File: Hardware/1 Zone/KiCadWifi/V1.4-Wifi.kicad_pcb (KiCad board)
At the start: 2 copper layers, 100 x 80 mm, 134 parts, among them CN11 Pinheader 1x02 P2.54 Horizont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, CN16 Pinheader 1x02 P2.54 Horizont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, Q1 AOD4184A, Q10 PJA3404A, Q11 PJA3404A, Q12 BC816-16VL, Q8 UMH3NTN, SW1 K2-1102DP-G3SW-04, SW2 K2-1102DP-G3SW-04, SW3 K2-1102DP-G3SW-04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

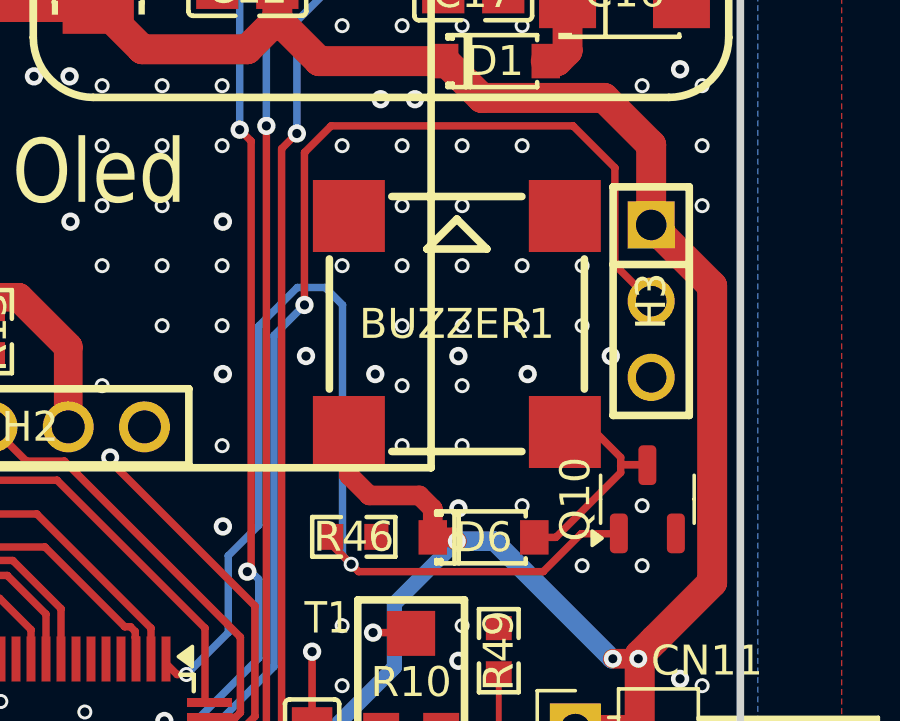
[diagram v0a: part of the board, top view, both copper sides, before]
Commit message: Replace Buzzer1 with CMT-8504-100-SMT-TR
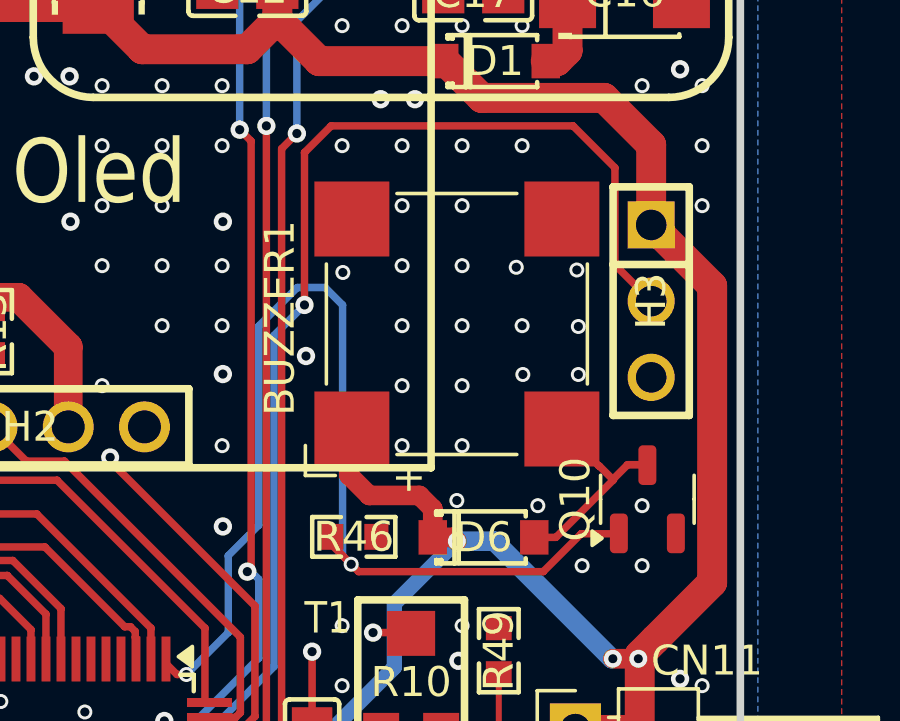
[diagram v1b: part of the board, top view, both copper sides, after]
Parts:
- BUZZER1: footprint V1.4-Wifi-easyedapro:BUZ-SMD_4P-L8.5-W8.5-P8.50-BR -> Buzzer_Beeper:MagneticBuzzer_CUI_CMT-8504-100-SMT
- turned BUZZER1 to 90 degrees
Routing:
- net THERMISTOR3: vias 2 -> 0

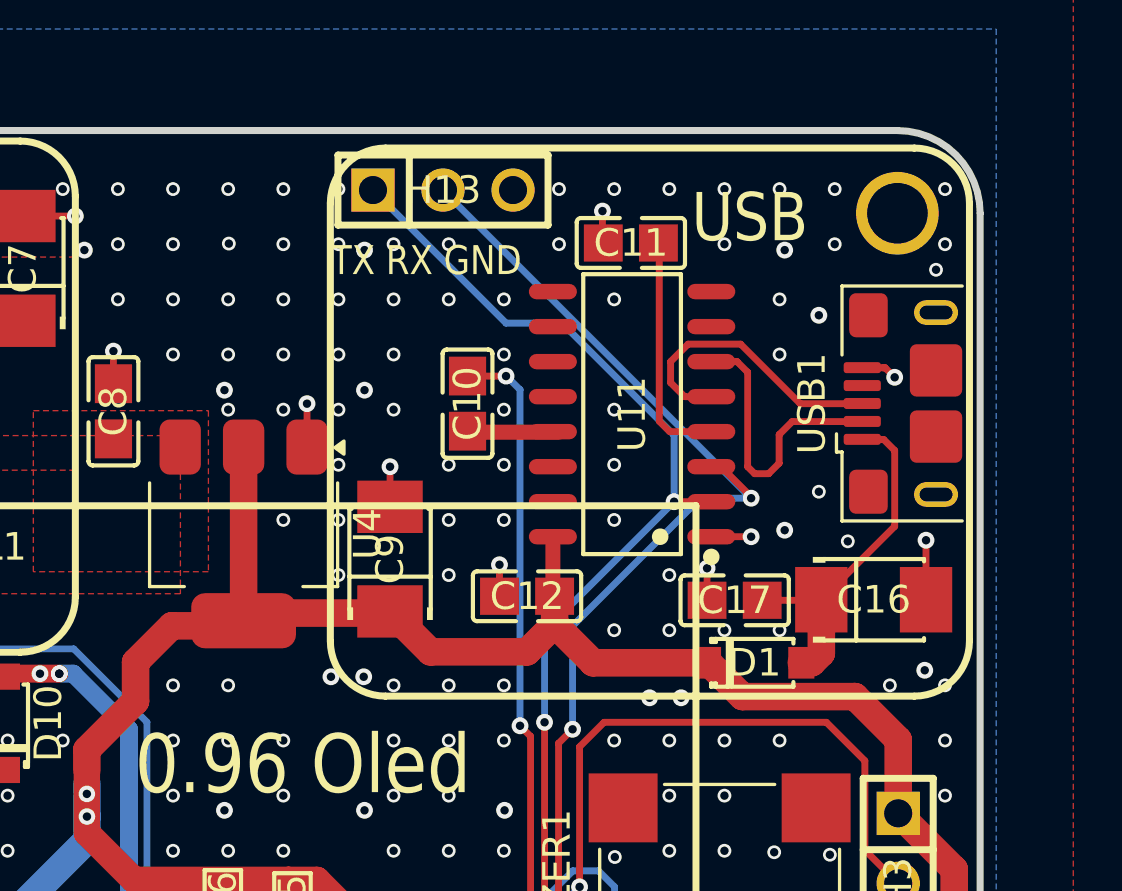
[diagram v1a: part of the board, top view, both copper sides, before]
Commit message: Reroute (minor), moved via and silkscreen apart, in USB area
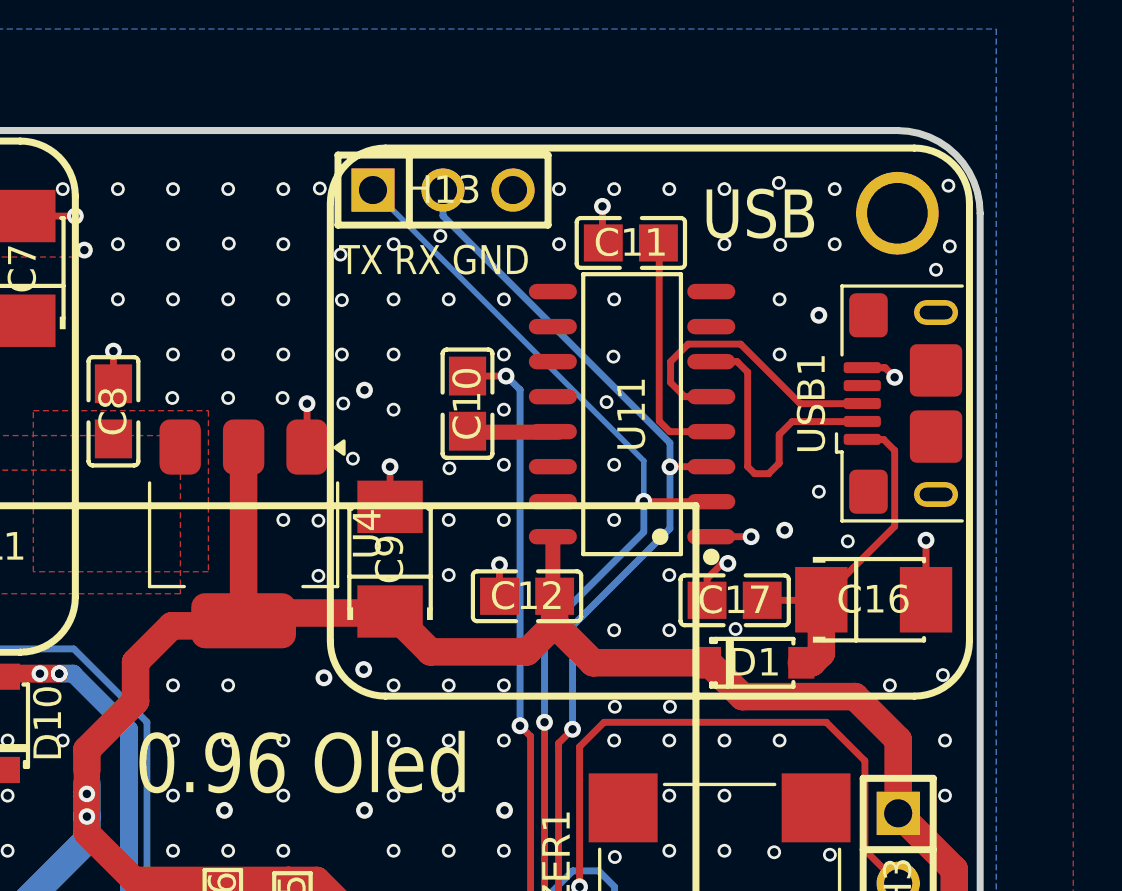
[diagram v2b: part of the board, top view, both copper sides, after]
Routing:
- net RXD: track 53.1 -> 49.1 mm
- net TXD: track 50.7 -> 49.7 mm
- net GND: track 77.0 -> 77.8 mm, vias 701 -> 699

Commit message: Changed R1,R2 and all 10K resistors to 0805. Fixed comment for C28.
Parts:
- C28: value 100nF 0603 -> 100nF 0805
- R1, R18, R2, R24, R29, R3, R30, R31, R32, R33, R35, R36, R37, R38, R46, R48: footprint V1.4-Wifi-easyedapro:R0603 -> Resistor_SMD:R_0805_2012Metric_Pad1.20x1.40mm_HandSolder
- turned R46 to 180 degrees
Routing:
- net +5V: track 355.4 -> 358.9 mm
- net THERMISTOR1: track 60.3 -> 61.1 mm

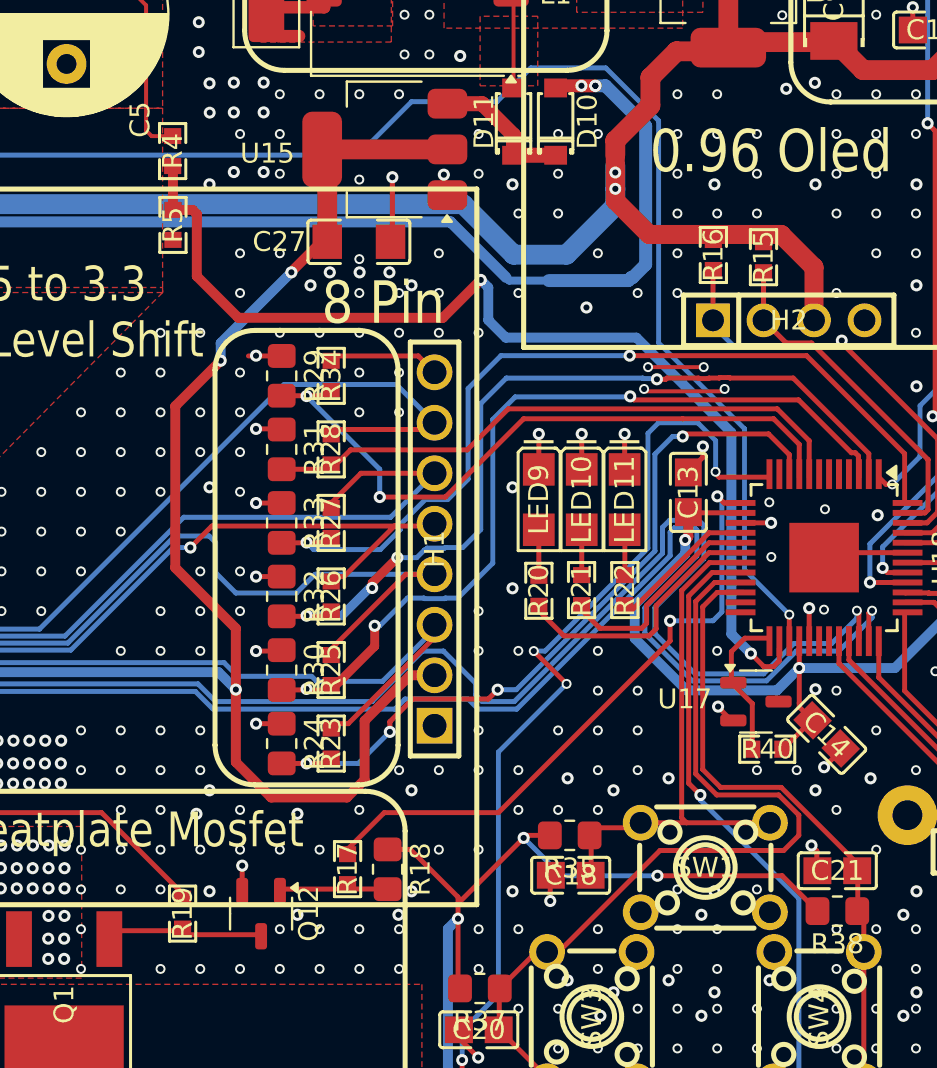
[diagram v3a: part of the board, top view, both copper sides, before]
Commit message: Changed all 4K7 resistors to 0805.
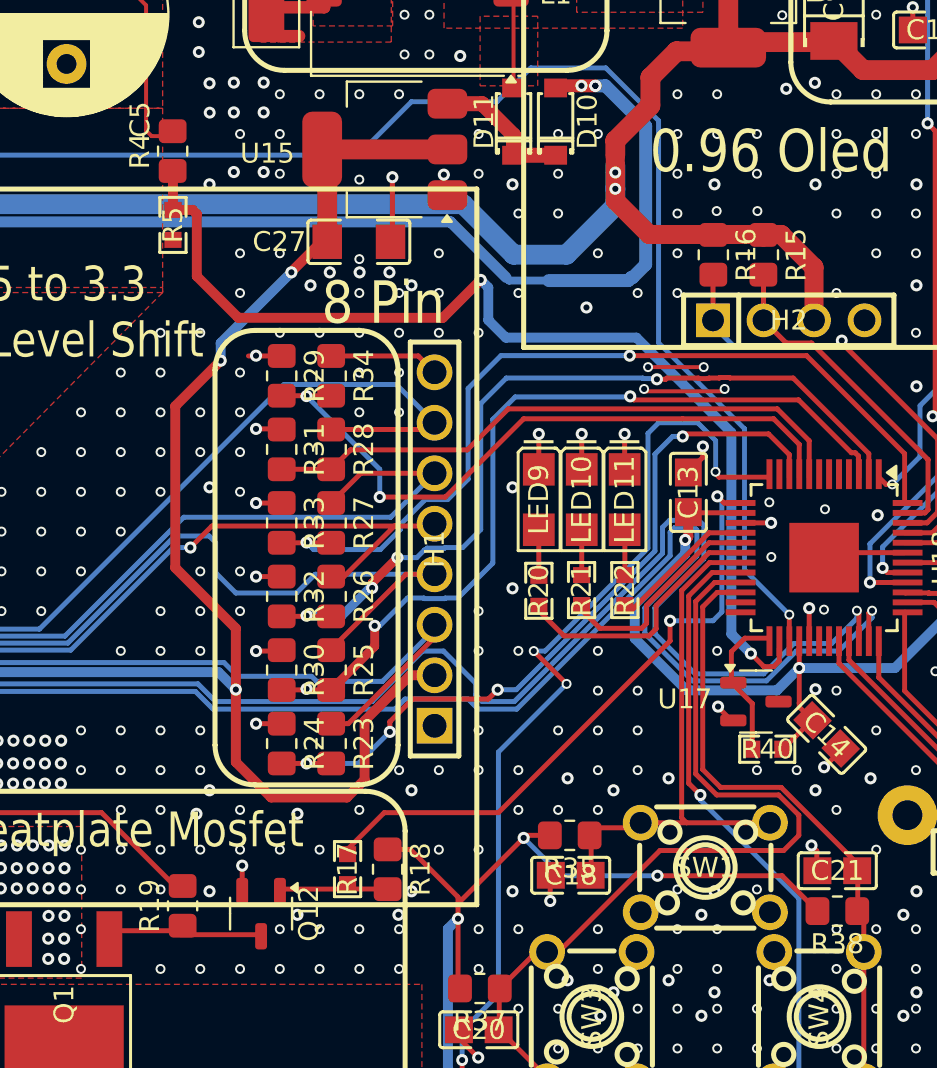
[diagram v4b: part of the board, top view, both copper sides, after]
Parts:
- R15, R16, R19, R23, R25, R26, R27, R28, R34, R4: footprint V1.4-Wifi-easyedapro:R0603 -> Resistor_SMD:R_0805_2012Metric_Pad1.20x1.40mm_HandSolder
- moved R19 0.39 mm to (145.8, 130.9)
- moved R15 0.12 mm to (175.1, 98.2)

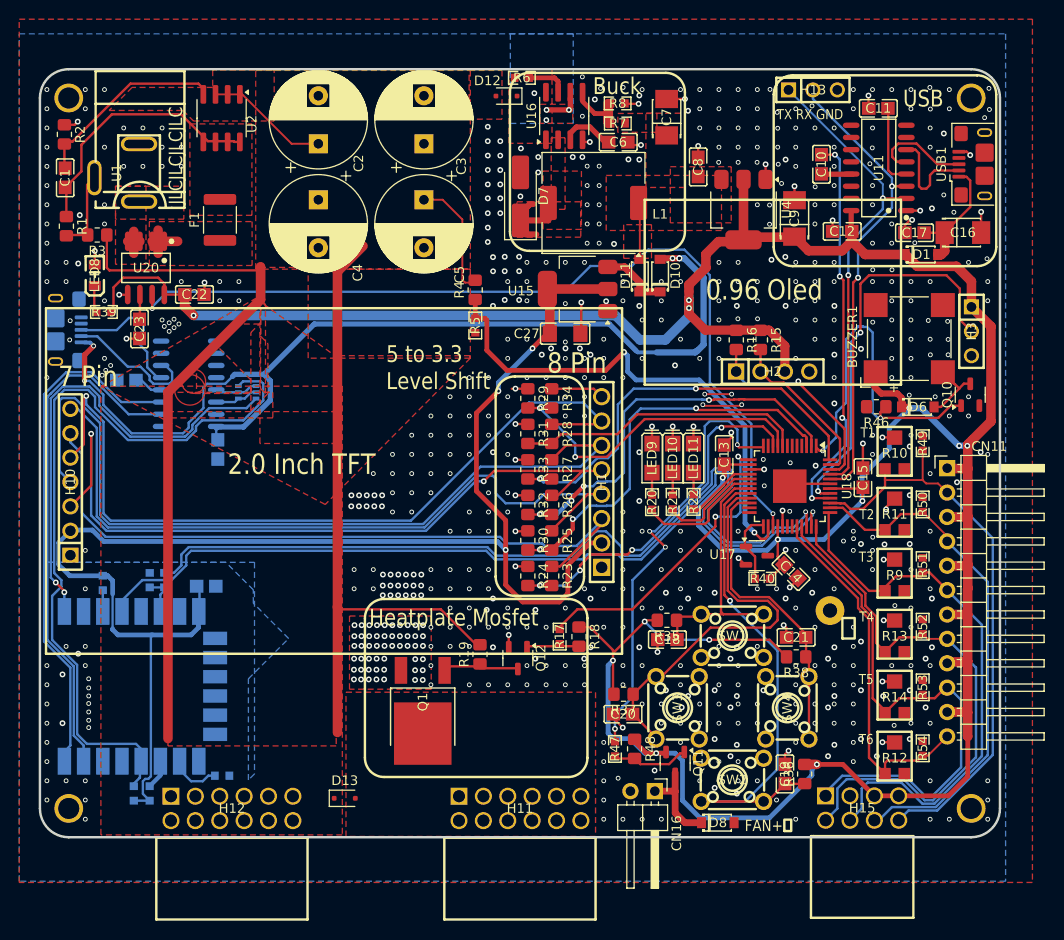
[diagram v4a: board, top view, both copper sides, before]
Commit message: Changed all 1K resistors to 0805. Moved R39 and LED8 a little.
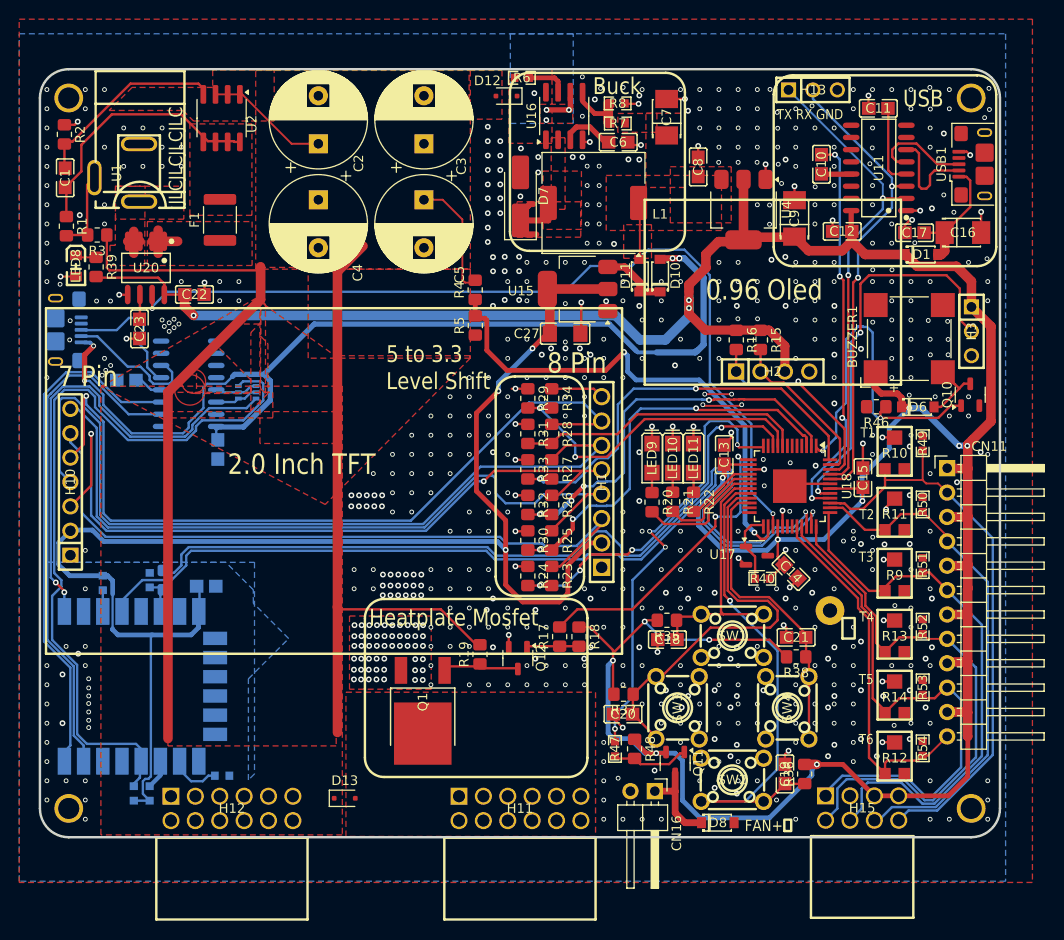
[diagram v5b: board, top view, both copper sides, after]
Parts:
- R17, R20, R21, R22, R39, R44, R5: footprint V1.4-Wifi-easyedapro:R0603 -> Resistor_SMD:R_0805_2012Metric_Pad1.20x1.40mm_HandSolder
- moved R39 4.76 mm to (105.8, 90.6), turned to -90 degrees
- moved LED8 2.19 mm to (103.8, 90.5), turned to -90 degrees
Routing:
- net +5V: track 358.9 -> 357.8 mm
- net Net-(LED8-A): track 2.75 -> 2.18 mm
- net GND: track 77.8 -> 77.9 mm, vias 699 -> 698
